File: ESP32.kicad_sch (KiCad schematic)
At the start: 17 parts, among them J7 Conn_01x05_Male, J8 Conn_01x05_Male, SW2 PTS810, SW3 PTS810, U4 ESP32-WROOM-32

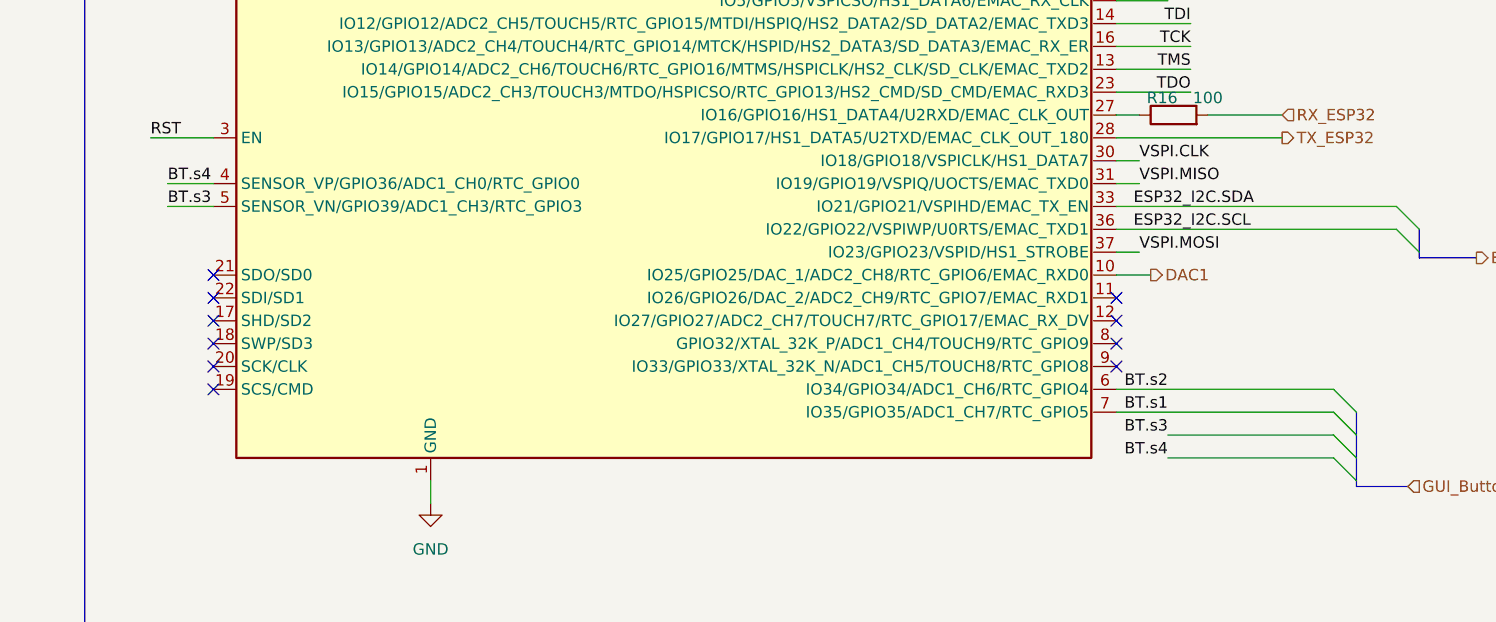
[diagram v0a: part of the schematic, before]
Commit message: finish some unconnect pins, draw edge cut board
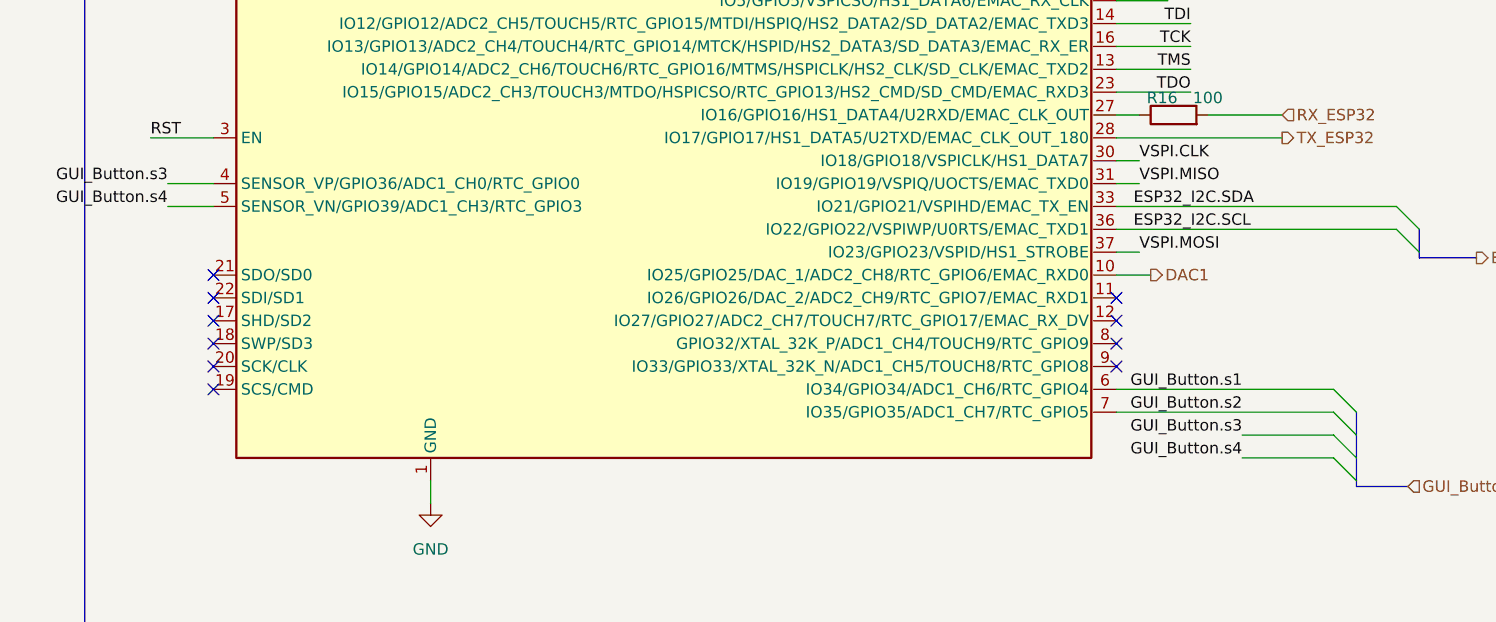
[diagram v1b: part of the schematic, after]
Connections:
- net BT.s1 renamed GUI_Button.s2
- net BT.s2 renamed GUI_Button.s1
- net BT.s3 renamed GUI_Button.s4
- net BT.s4 renamed GUI_Button.s3
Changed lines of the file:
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@@
 	(wire
 		(pts
-			(xy 131.445 121.285) (xy 149.86 121.285)
+			(xy 139.7 121.285) (xy 149.86 121.285)
 		)
 		(stroke
@@
 	(wire
 		(pts
-			(xy 131.445 123.825) (xy 149.86 123.825)
+			(xy 139.7 123.825) (xy 149.86 123.825)
 		)
 		(stroke
@@
 		)
 	)
-	(label "BT.s4"
-		(at 20.32 93.345 0)
-		(fields_autoplaced yes)
-		(effects
-			(font
-				(size 1.27 1.27)
-			)
-			(justify left bottom)
-		)
-	)
 	(label "VSPI.MOSI"
 		(at 128.27 100.965 0)
@@
 		)
 	)
+	(label "GUI_Button.s3"
+		(at 20.32 93.345 180)
+		(fields_autoplaced yes)
+		(effects
+			(font
+				(size 1.27 1.27)
+			)
+			(justify right bottom)
+		)
+	)
 	(label "VDD_ESP32"
 		(at 79.3496 38.1 180)
@@
 		)
 	)
-	(label "BT.s2"
-		(at 131.445 116.205 180)
+	(label "GUI_Button.s1"
+		(at 139.7 116.205 180)
 		(fields_autoplaced yes)
 		(effects
@@
 		)
 	)
+	(label "GUI_Button.s4"
+		(at 20.32 95.885 180)
+		(fields_autoplaced yes)
+		(effects
+			(font
+				(size 1.27 1.27)
+			)
+			(justify right bottom)
+		)
+	)
 	(label "ESP32_I2C.SDA"
 		(at 127.635 95.885 0)
@@
 		)
 	)
-	(label "BT.s1"
-		(at 131.445 118.745 180)
+	(label "GUI_Button.s2"
+		(at 139.7 118.745 180)
 		(fields_autoplaced yes)
 		(effects
@@
 		)
 	)
-	(label "BT.s3"
-		(at 20.32 95.885 0)
-		(fields_autoplaced yes)
-		(effects
-			(font
-				(size 1.27 1.27)
-			)
-			(justify left bottom)
-		)
-	)
-	(label "BT.s4"
-		(at 131.445 123.825 180)
+	(label "GUI_Button.s4"
+		(at 139.7 123.825 180)
 		(fields_autoplaced yes)
 		(effects
@@
 		)
 	)
-	(label "BT.s3"
-		(at 131.445 121.285 180)
-		(fields_autoplaced yes)
-		(effects
+	(label "GUI_Button.s3"
+		(at 139.7 121.285 180)
+		(fields_autoplaced yes)
+		(effects

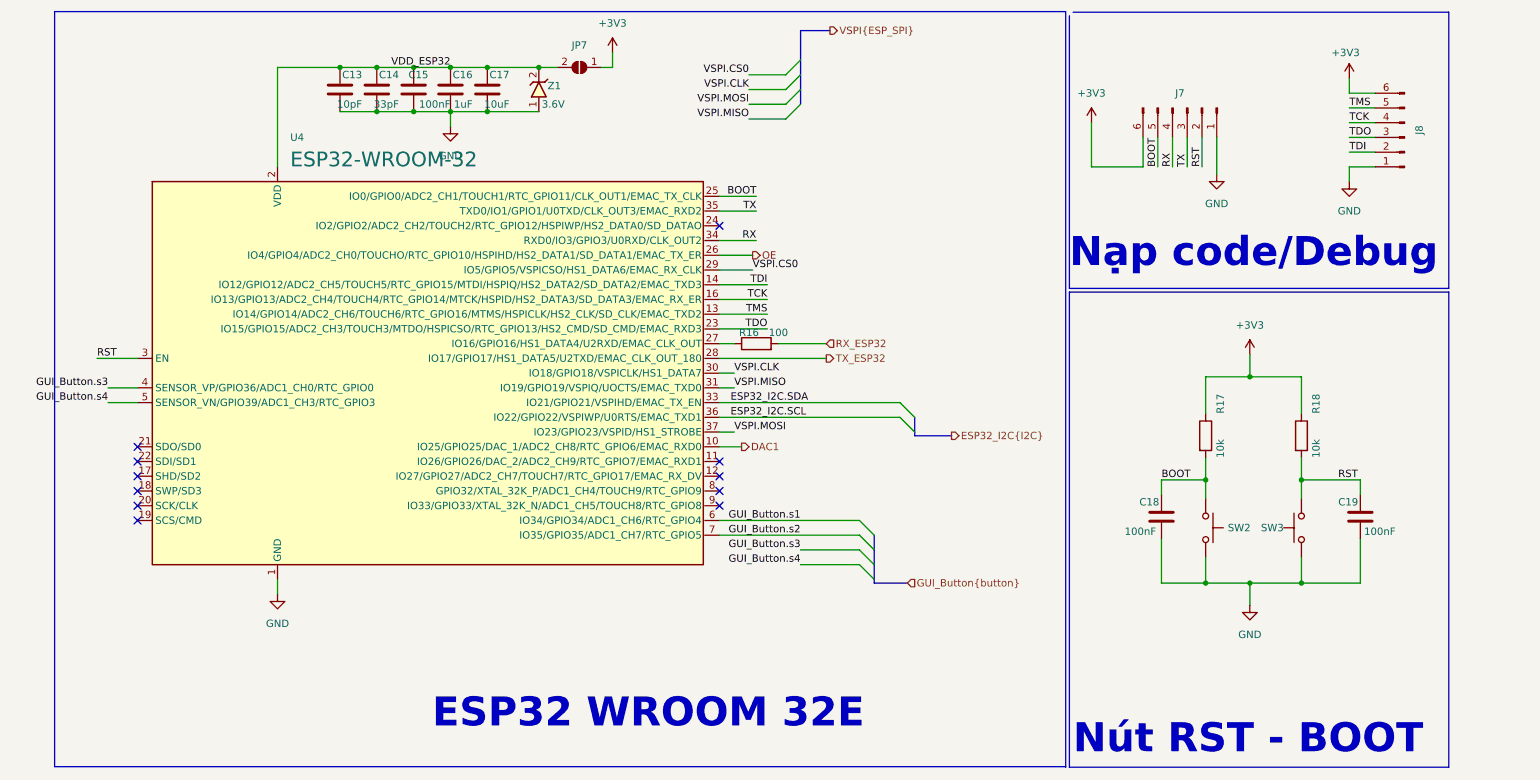
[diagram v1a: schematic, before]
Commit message: Add LORA, SDcard and Volt to 4_20mA scheamtic
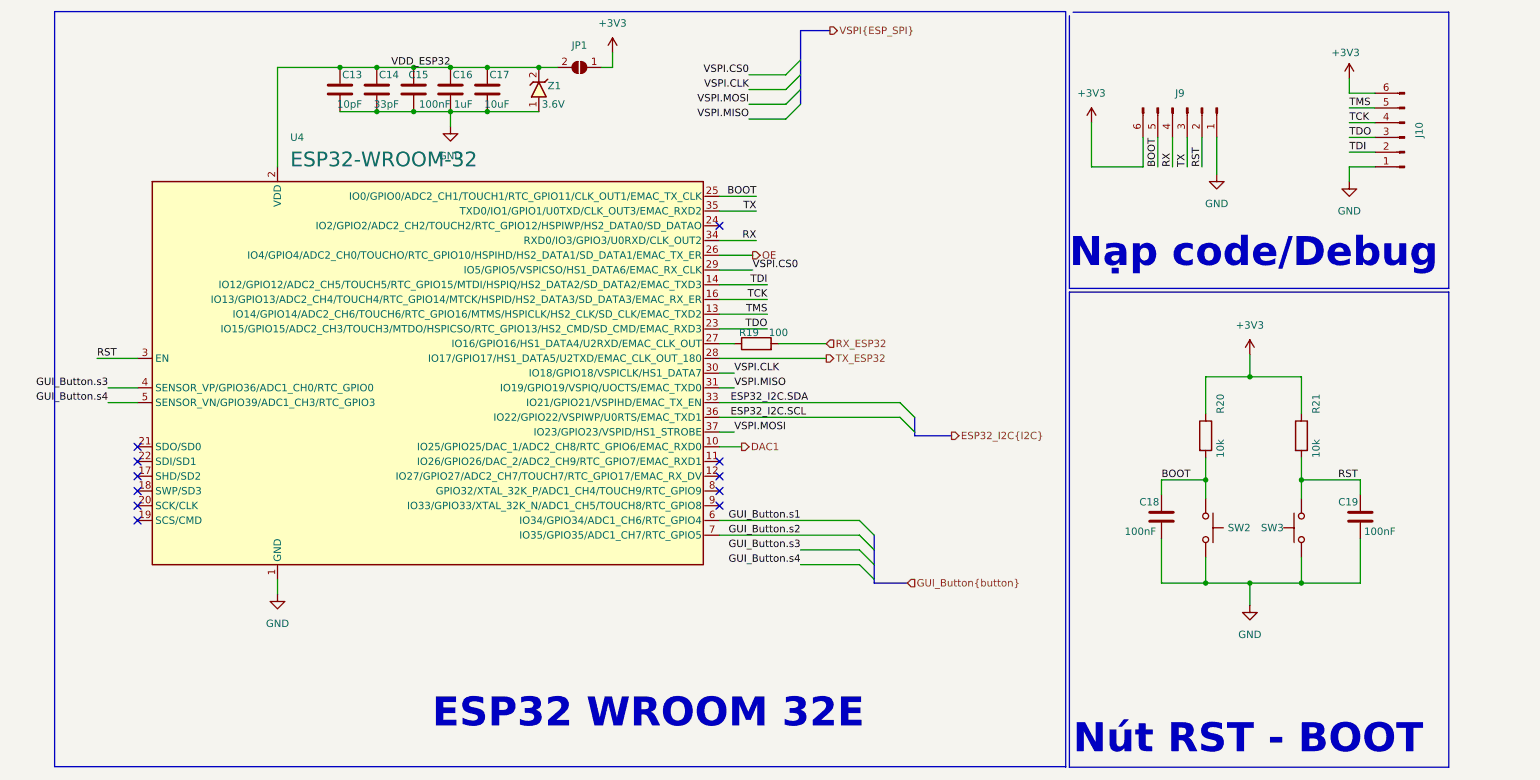
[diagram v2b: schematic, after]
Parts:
- renumbered J8 to J10, J7 to J9, JP7 to JP1, R16 to R19, R17 to R20, R18 to R21
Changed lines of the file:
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@@
 		(on_board yes)
 		(dnp no)
-		(property "Reference" "R16"
+		(property "Reference" "R19"
 			(at 130.81 83.82 90)
 			(effects
@@
 			(project "DongTamV2"
 				(path "/2303d546-b88a-4ab0-aee1-26e3b32ac9d7/abf795b6-a215-4309-99bc-ba882add59d7"
-					(reference "R16")
+					(reference "R19")
 					(unit 1)
 				)
@@
 		(on_board yes)
 		(dnp no)
-		(property "Reference" "#PWR017"
+		(property "Reference" "#PWR029"
 			(at 234.315 43.815 0)
 			(effects
@@
 			(project "DongTamV2"
 				(path "/2303d546-b88a-4ab0-aee1-26e3b32ac9d7/abf795b6-a215-4309-99bc-ba882add59d7"
-					(reference "#PWR017")
+					(reference "#PWR029")
 					(unit 1)
 				)
@@
 		(dnp no)
 		(fields_autoplaced yes)
-		(property "Reference" "#PWR016"
+		(property "Reference" "#PWR028"
 			(at 217.17 137.16 0)
 			(effects
@@
 			(project "DongTamV2"
 				(path "/2303d546-b88a-4ab0-aee1-26e3b32ac9d7/abf795b6-a215-4309-99bc-ba882add59d7"
-					(reference "#PWR016")
+					(reference "#PWR028")
 					(unit 1)
 				)
@@
 		(dnp no)
 		(fields_autoplaced yes)
-		(property "Reference" "#PWR012"
+		(property "Reference" "#PWR024"
 			(at 107.2896 39.37 0)
 			(effects
@@
 			(project "DongTamV2"
 				(path "/2303d546-b88a-4ab0-aee1-26e3b32ac9d7/abf795b6-a215-4309-99bc-ba882add59d7"
-					(reference "#PWR012")
+					(reference "#PWR024")
 					(unit 1)
 				)
@@
 		(dnp no)
 		(fields_autoplaced yes)
-		(property "Reference" "#PWR015"
+		(property "Reference" "#PWR027"
 			(at 217.17 91.44 0)
 			(effects
@@
 			(project "DongTamV2"
 				(path "/2303d546-b88a-4ab0-aee1-26e3b32ac9d7/abf795b6-a215-4309-99bc-ba882add59d7"
-					(reference "#PWR015")
+					(reference "#PWR027")
 					(unit 1)
 				)
@@
 		(dnp no)
 		(fields_autoplaced yes)
-		(property "Reference" "#PWR013"
+		(property "Reference" "#PWR025"
 			(at 189.865 51.435 0)
 			(effects
@@
 			(project "DongTamV2"
 				(path "/2303d546-b88a-4ab0-aee1-26e3b32ac9d7/abf795b6-a215-4309-99bc-ba882add59d7"
-					(reference "#PWR013")
+					(reference "#PWR025")
 					(unit 1)
 				)
@@
 		(on_board yes)
 		(dnp no)
-		(property "Reference" "R18"
+		(property "Reference" "R21"
 			(at 228.6 97.79 90)
 			(effects
@@
 			(project "DongTamV2"
 				(path "/2303d546-b88a-4ab0-aee1-26e3b32ac9d7/abf795b6-a215-4309-99bc-ba882add59d7"
-					(reference "R18")
+					(reference "R21")
 					(unit 1)
 				)
@@
 		(on_board yes)
 		(dnp no)
-		(property "Reference" "#PWR011"
+		(property "Reference" "#PWR023"
 			(at 79.3496 54.61 0)
 			(effects
@@
 			(project "DongTamV2"
 				(path "/2303d546-b88a-4ab0-aee1-26e3b32ac9d7/abf795b6-a215-4309-99bc-ba882add59d7"
-					(reference "#PWR011")
+					(reference "#PWR023")
 					(unit 1)
 				)
@@
 		(dnp no)
 		(fields_autoplaced yes)
-		(property "Reference" "JP7"
+		(property "Reference" "JP1"
 			(at 101.5746 34.29 0)
 			(effects
@@
 			(project "DongTamV2"
 				(path "/2303d546-b88a-4ab0-aee1-26e3b32ac9d7/abf795b6-a215-4309-99bc-ba882add59d7"
-					(reference "JP7")
+					(reference "JP1")
 					(unit 1)
 				)
@@
 		(dnp no)
 		(fields_autoplaced yes)
-		(property "Reference" "#PWR018"
+		(property "Reference" "#PWR030"
 			(at 234.315 64.135 0)
 			(effects
@@
 			(project "DongTamV2"
 				(path "/2303d546-b88a-4ab0-aee1-26e3b32ac9d7/abf795b6-a215-4309-99bc-ba882add59d7"
-					(reference "#PWR018")
+					(reference "#PWR030")
 					(unit 1)
 				)
@@
 		(on_board yes)
 		(dnp no)
-		(property "Reference" "R17"
+		(property "Reference" "R20"
 			(at 212.09 97.79 90)
 			(effects
@@
 			(project "DongTamV2"
 				(path "/2303d546-b88a-4ab0-aee1-26e3b32ac9d7/abf795b6-a215-4309-99bc-ba882add59d7"
-					(reference "R17")
+					(reference "R20")
 					(unit 1)
 				)
@@
 		(dnp no)
 		(fields_autoplaced yes)
-		(property "Reference" "J7"
+		(property "Reference" "J9"
 			(at 205.105 42.545 90)
 			(effects
@@
 			(project "DongTamV2"
 				(path "/2303d546-b88a-4ab0-aee1-26e3b32ac9d7/abf795b6-a215-4309-99bc-ba882add59d7"
-					(reference "J7")
+					(reference "J9")
 					(unit 1)
 				)
@@
 		(dnp no)
 		(fields_autoplaced yes)
-		(property "Reference" "J8"
+		(property "Reference" "J10"
 			(at 246.38 48.895 90)
 			(effects
@@
 			(project "DongTamV2"
 				(path "/2303d546-b88a-4ab0-aee1-26e3b32ac9d7/abf795b6-a215-4309-99bc-ba882add59d7"
-					(reference "J8")
+					(reference "J10")
 					(unit 1)
 				)
@@
 		(dnp no)
 		(fields_autoplaced yes)
-		(property "Reference" "#PWR014"
+		(property "Reference" "#PWR026"
 			(at 211.455 62.865 0)
 			(effects
@@
 			(project "DongTamV2"
 				(path "/2303d546-b88a-4ab0-aee1-26e3b32ac9d7/abf795b6-a215-4309-99bc-ba882add59d7"
-					(reference "#PWR014")
+					(reference "#PWR026")
 					(unit 1)
 				)
@@
 		(dnp no)
 		(fields_autoplaced yes)
-		(property "Reference" "#PWR010"
+		(property "Reference" "#PWR022"
 			(at 49.53 135.255 0)
 			(effects
@@
 			(project "DongTamV2"
 				(path "/2303d546-b88a-4ab0-aee1-26e3b32ac9d7/abf795b6-a215-4309-99bc-ba882add59d7"
-					(reference "#PWR010")
-					(unit 1)
-				)
+					(reference "#PWR022")
+					(unit 1)
+				)

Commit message: layout p1
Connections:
- net +3V3 renamed +3.3V
